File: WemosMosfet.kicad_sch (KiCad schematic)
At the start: 10 parts, among them J1 MIST, J2 ADC_1, J3 KEY_2, J4 KEY_1, Q3 BSS138, U1 WeMos_D1_mini

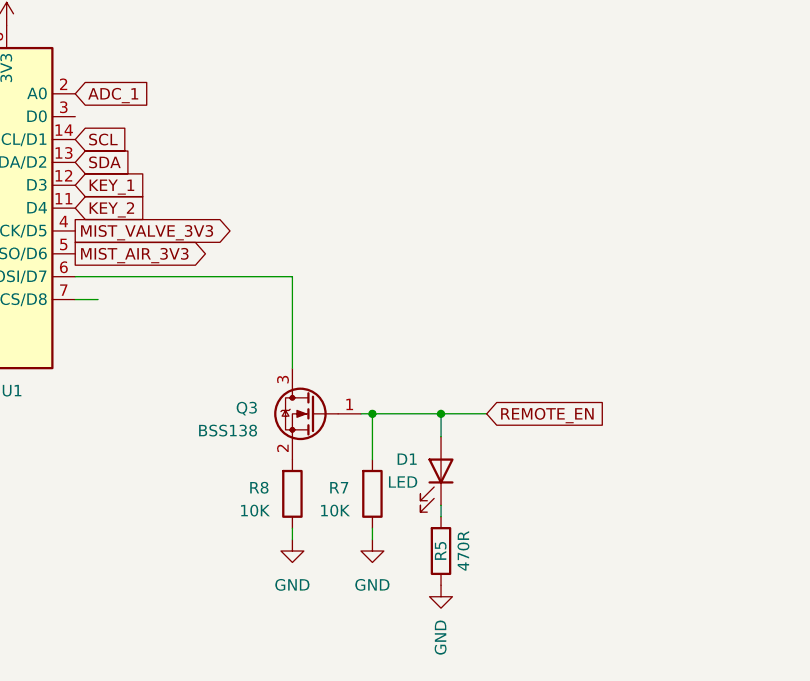
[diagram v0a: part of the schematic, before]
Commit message: Fixed some design flaws, first version didn't work.
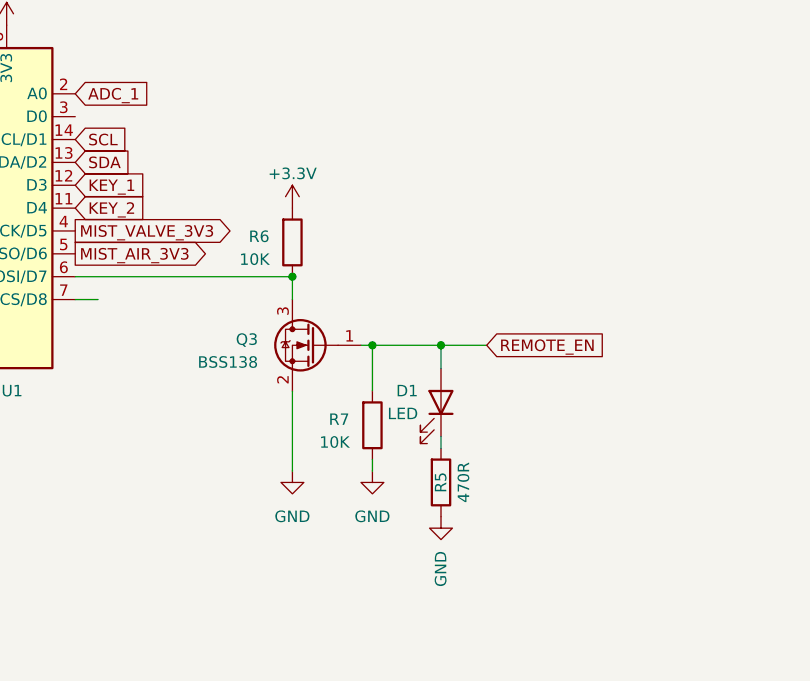
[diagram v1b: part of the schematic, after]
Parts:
- removed R8: 10K, Resistor_SMD:R_0805_2012Metric_Pad1.20x1.40mm_HandSolder, symbol Device:R
- added R6: 10K, Resistor_SMD:R_0805_2012Metric_Pad1.20x1.40mm_HandSolder, symbol Device:R
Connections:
- net +3.3V: now also R6.2
- net GND: now also Q3.2 (S)
- net at Q3.3 (D), U1.6 (MOSI/D7): now also R6.1
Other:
- moved on the sheet: D1, Q3, R5, R7
